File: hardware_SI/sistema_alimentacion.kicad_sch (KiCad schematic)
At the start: 29 parts

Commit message: Etq compon, C desacop, ferrita
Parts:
- added C9: 100n, symbol Device:C
- added FB1: FerriteBead, symbol Device:FerriteBead
- R10: renamed from R?; value R -> 1.5M
- R11: renamed from R?; value R -> 180k
- gave numbers to parts that had none: 27
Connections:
- net +BATT: now also C9.1
- net GND: now also J2.5 (GND), C9.2, FB1.2
- net GNDPWR: now also FB1.1; no longer J2.5 (GND)

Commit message: mod_WD, etiquetas y clocks
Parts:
- added FB?: FerriteBead, Resistor_SMD:R_0805_2012Metric_Pad1.20x1.40mm_HandSolder, symbol Device:FerriteBead
- FB1: footprint (none) -> Resistor_SMD:R_0805_2012Metric_Pad1.20x1.40mm_HandSolder
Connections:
- net GND: now also FB?.1
- net GNDPWR: now also FB?.2
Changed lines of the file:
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@@
   (junction (at 148.59 157.48) (diameter 0) (color 0 0 0 0)
+  )
+  (junction (at 113.03 185.42) (diameter 0) (color 0 0 0 0)
+  )
+  (junction (at 105.41 185.42) (diameter 0) (color 0 0 0 0)
   )
   (junction (at 137.16 167.64) (diameter 0) (color 0 0 0 0)
@@
     (stroke (width 0) (type default) (color 0 0 0 0))
   )
-  (wire (pts (xy 113.03 177.8) (xy 113.03 176.53))
+  (wire (pts (xy 113.03 185.42) (xy 113.03 176.53))
+    (stroke (width 0) (type default) (color 0 0 0 0))
+  )
+  (wire (pts (xy 113.03 189.23) (xy 113.03 185.42))
     (stroke (width 0) (type default) (color 0 0 0 0))
   )
@@
     (stroke (width 0) (type default) (color 0 0 0 0))
   )
+  (wire (pts (xy 105.41 185.42) (xy 105.41 189.23))
+    (stroke (width 0) (type default) (color 0 0 0 0))
+  )
   (wire (pts (xy 83.82 52.07) (xy 86.36 52.07))
     (stroke (width 0) (type default) (color 0 0 0 0))
@@
     (stroke (width 0) (type default) (color 0 0 0 0))
   )
-  (wire (pts (xy 105.41 176.53) (xy 105.41 177.8))
+  (wire (pts (xy 105.41 176.53) (xy 105.41 185.42))
     (stroke (width 0) (type default) (color 0 0 0 0))
   )
@@
       (effects (font (size 1.27 1.27)) (justify left bottom) hide)
     )
-    (property "Datasheet" "" (id 3) (at 86.36 49.53 0)
+    (property "Datasheet" "https://co.mouser.com/datasheet/2/609/4085fd-1268485.pdf" (id 3) (at 86.36 49.53 0)
       (effects (font (size 1.27 1.27)) (justify left bottom) hide)
     )
@@
     (pin "3")
   )
+  (symbol (lib_id "Device:FerriteBead") (at 109.22 185.42 90) (unit 1)
+    (in_bom yes) (on_board yes)
+    (property "Reference" "FB?" (id 0) (at 109.1692 177.8 90))
+    (property "Value" "FerriteBead" (id 1) (at 109.1692 180.34 90))
+    (property "Footprint" "Resistor_SMD:R_0805_2012Metric_Pad1.20x1.40mm_HandSolder" (id 2) (at 109.22 187.198 90)
+      (effects (font (size 1.27 1.27)) hide)
+    )
+    (property "Datasheet" "https://co.mouser.com/datasheet/2/396/TaiyoYuden_chipbeads01_e-1274227.pdf" (id 3) (at 109.22 185.42 0)
+      (effects (font (size 1.27 1.27)) hide)
+    )
+    (pin "1")
+    (pin "2")
+  )
   (symbol (lib_id "Device:FerriteBead") (at 62.23 135.89 90) (unit 1)
     (in_bom yes) (on_board yes)
     (property "Reference" "FB1" (id 0) (at 62.1792 128.27 90))
     (property "Value" "FerriteBead" (id 1) (at 62.1792 130.81 90))
-    (property "Footprint" "" (id 2) (at 62.23 137.668 90)
-      (effects (font (size 1.27 1.27)) hide)
-    )
-    (property "Datasheet" "~" (id 3) (at 62.23 135.89 0)
+    (property "Footprint" "Resistor_SMD:R_0805_2012Metric_Pad1.20x1.40mm_HandSolder" (id 2) (at 62.23 137.668 90)
+      (effects (font (size 1.27 1.27)) hide)
+    )
+    (property "Datasheet" "https://co.mouser.com/datasheet/2/396/TaiyoYuden_chipbeads01_e-1274227.pdf" (id 3) (at 62.23 135.89 0)
       (effects (font (size 1.27 1.27)) hide)
     )
@@
     (pin "2")
   )
-  (symbol (lib_id "power:GND") (at 105.41 177.8 0) (unit 1)
-    (in_bom yes) (on_board yes)
-    (property "Reference" "#PWR?" (id 0) (at 105.41 184.15 0)
-      (effects (font (size 1.27 1.27)) hide)
-    )
-    (property "Value" "GND" (id 1) (at 105.41 181.61 0))
-    (property "Footprint" "" (id 2) (at 105.41 177.8 0)
-      (effects (font (size 1.27 1.27)) hide)
-    )
-    (property "Datasheet" "" (id 3) (at 105.41 177.8 0)
+  (symbol (lib_id "power:GND") (at 105.41 189.23 0) (unit 1)
+    (in_bom yes) (on_board yes)
+    (property "Reference" "#PWR?" (id 0) (at 105.41 195.58 0)
+      (effects (font (size 1.27 1.27)) hide)
+    )
+    (property "Value" "GND" (id 1) (at 105.41 193.04 0))
+    (property "Footprint" "" (id 2) (at 105.41 189.23 0)
+      (effects (font (size 1.27 1.27)) hide)
+    )
+    (property "Datasheet" "" (id 3) (at 105.41 189.23 0)
       (effects (font (size 1.27 1.27)) hide)
     )
@@
     (pin "1")
   )
-  (symbol (lib_id "power:GNDPWR") (at 113.03 177.8 0) (unit 1)
-    (in_bom yes) (on_board yes)
-    (property "Reference" "#PWR?" (id 0) (at 113.03 182.88 0)
-      (effects (font (size 1.27 1.27)) hide)
-    )
-    (property "Value" "GNDPWR" (id 1) (at 113.03 181.61 0))
-    (property "Footprint" "" (id 2) (at 113.03 179.07 0)
-      (effects (font (size 1.27 1.27)) hide)
-    )
-    (property "Datasheet" "" (id 3) (at 113.03 179.07 0)
-      (effects (font (size 1.27 1.27)) hide)
-    )
+  (symbol (lib_id "power:GNDPWR") (at 113.03 189.23 0) (unit 1)
+    (in_bom yes) (on_board yes)
+    (property "Reference" "#PWR?" (id 0) (at 113.03 194.31 0)
+      (effects (font (size 1.27 1.27)) hide)
+    )
+    (property "Value" "GNDPWR" (id 1) (at 113.03 193.04 0))
+    (property "Footprint" "" (id 2) (at 113.03 190.5 0)
+      (effects (font (size 1.27 1.27)) hide)
+    )
+    (property "Datasheet" "" (id 3) (at 113.03 190.5 0)
+      (effects (font (size 1.27 1.27)) hide)
+    )

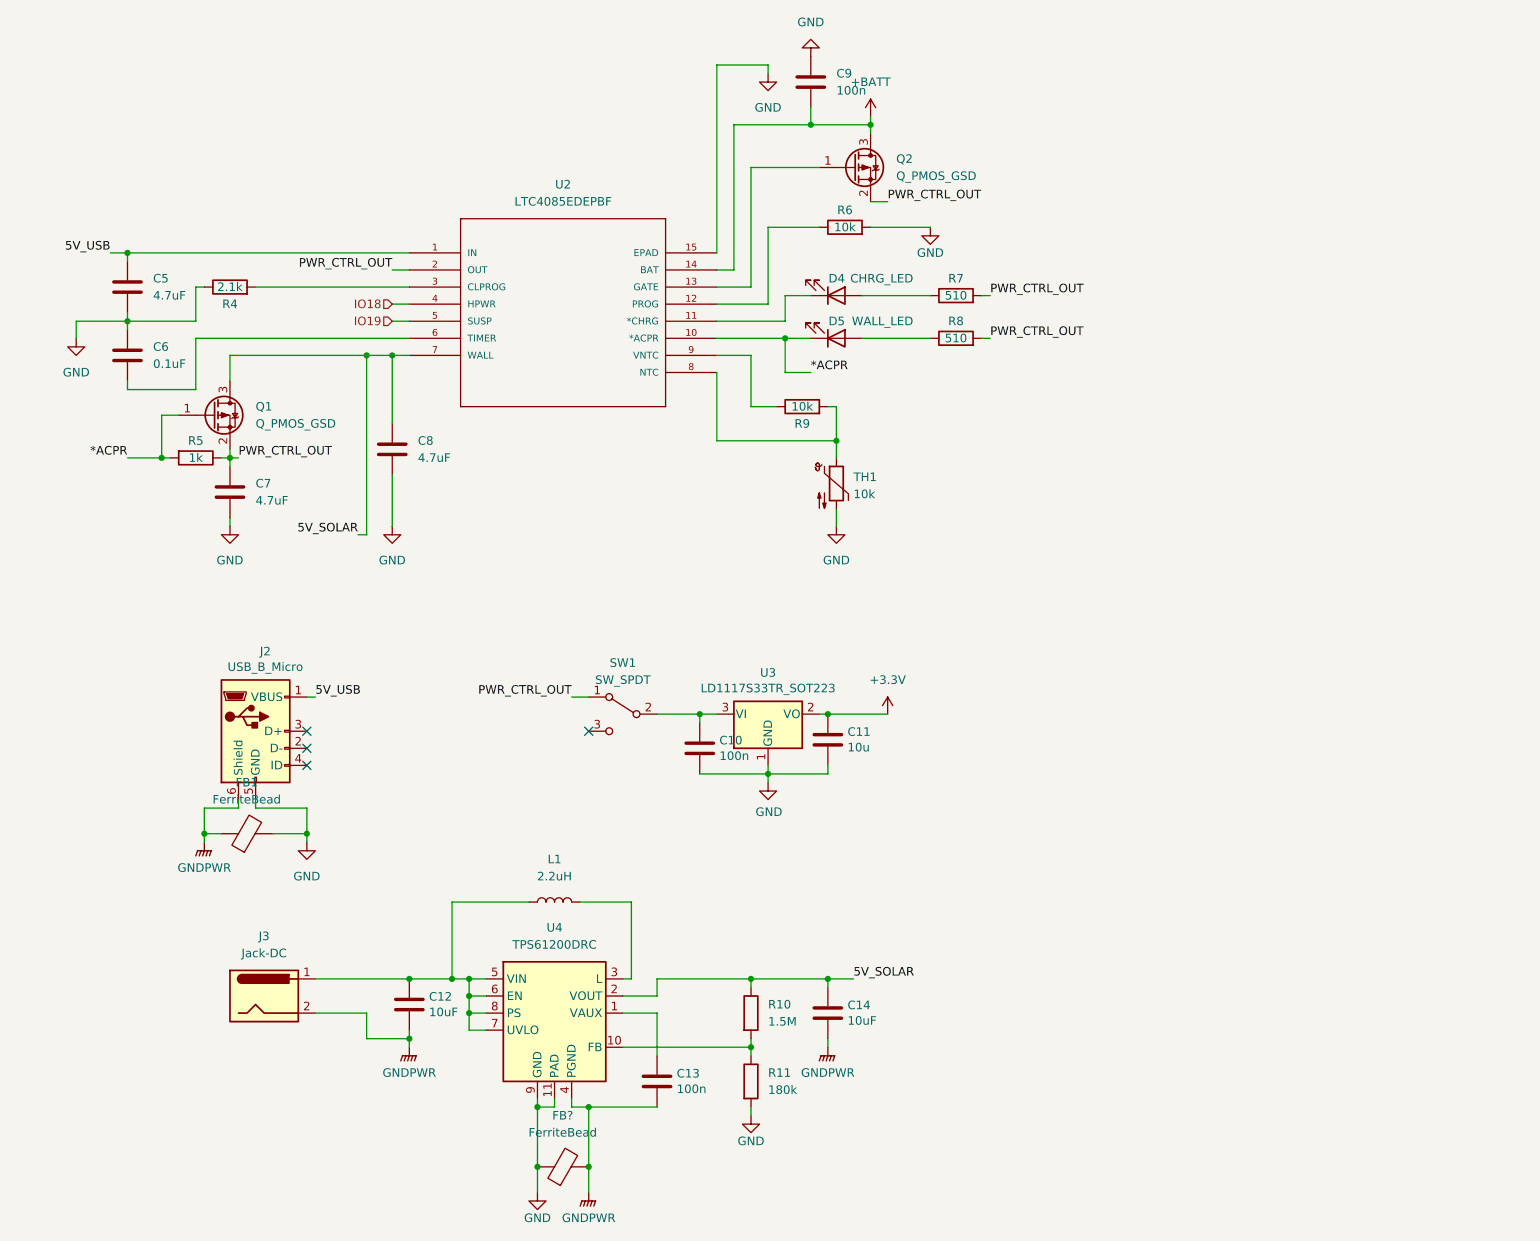
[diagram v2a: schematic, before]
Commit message: USB Serial, huellas y correcciones ERC
- Se agregaron componentes para la comunicación serial con la Omega2+.
- Se actualizaron huellas en función de la disponibilidad de los componentes.
- Se ejecutó el ERC y se solucionaron los errores mostrados.
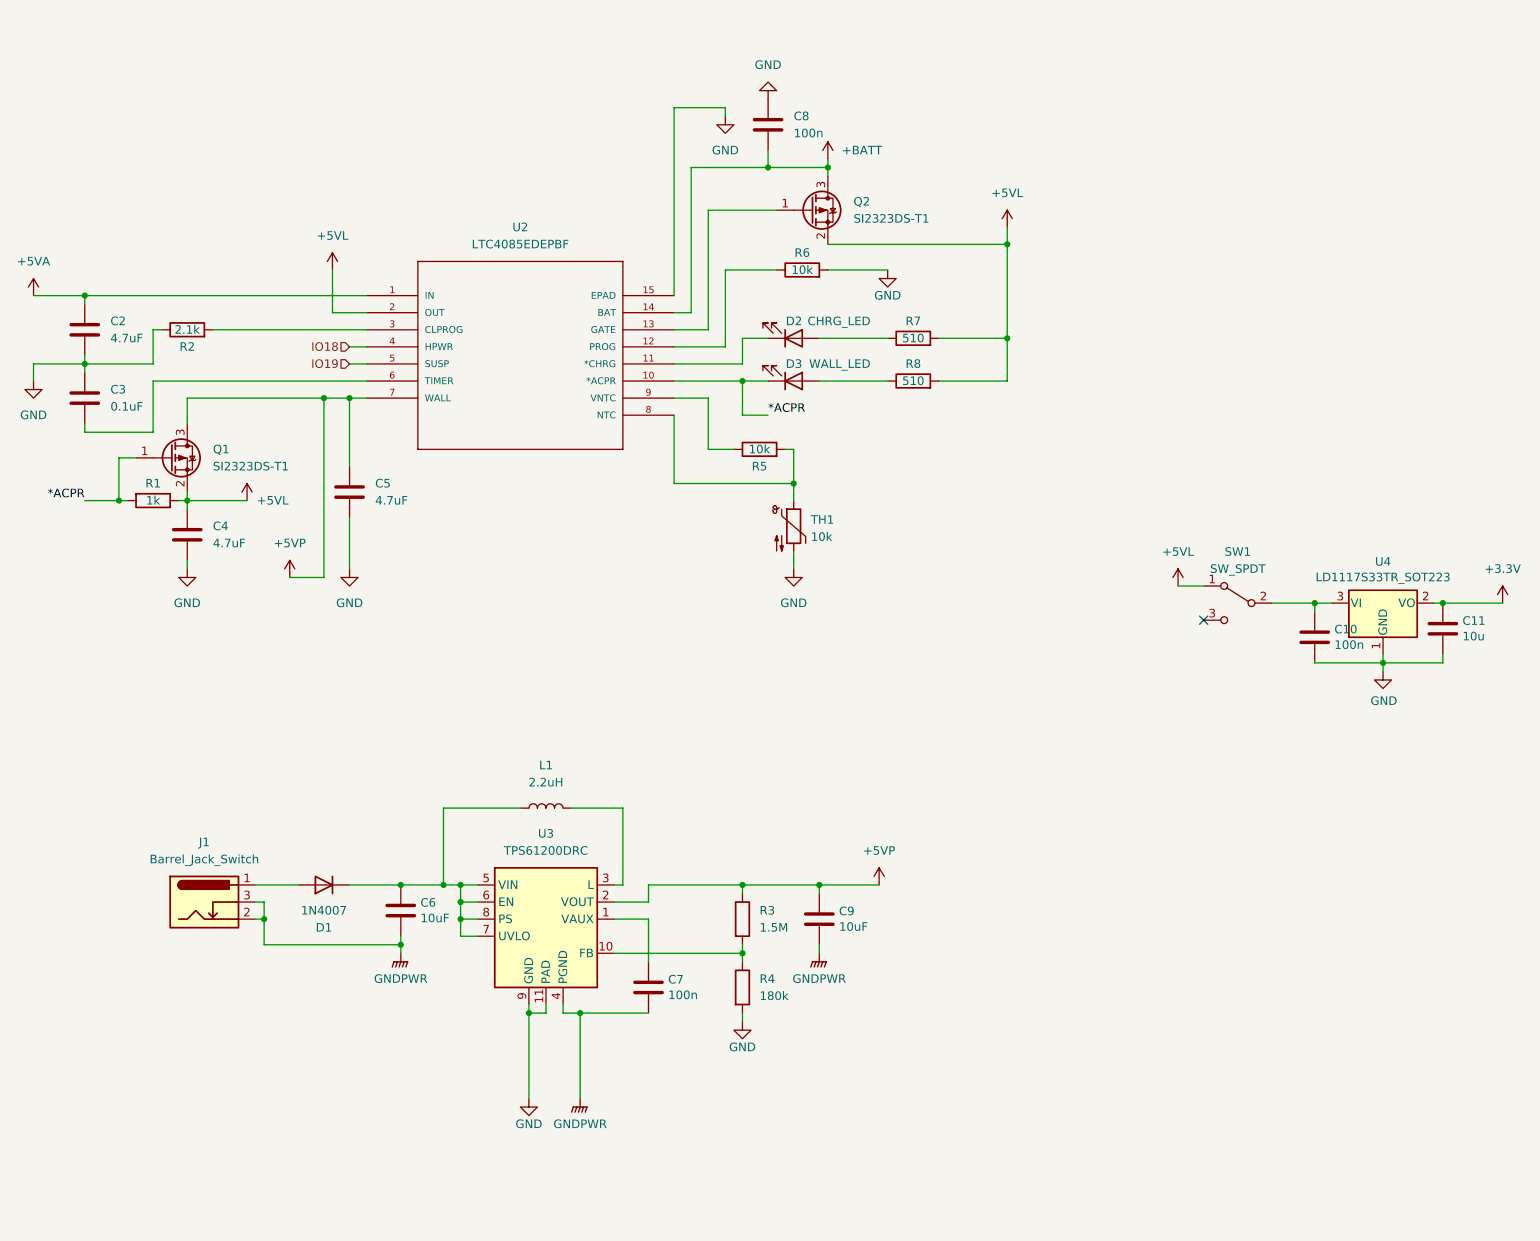
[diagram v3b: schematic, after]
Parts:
- removed FB1, FB?: FerriteBead, Resistor_SMD:R_0805_2012Metric_Pad1.20x1.40mm_HandSolder, symbol Device:FerriteBead
- removed J2: USB_B_Micro, Connector_USB:USB_Micro-B_Molex-105017-0001, symbol Connector:USB_B_Micro
- removed J3: Jack-DC, Connector_BarrelJack:BarrelJack_SwitchcraftConxall_RAPC10U_Horizontal, symbol Connector:Jack-DC
- added D1: 1N4007, Diode_SMD:D_SMA_Handsoldering, symbol Diode:1N4007
- added J1: Barrel_Jack_Switch, Connector_BarrelJack:BarrelJack_Horizontal, symbol Connector:Barrel_Jack_Switch
- Q1, Q2: value Q_PMOS_GSD -> SI2323DS-T1
- renumbered C5 to C2, C6 to C3, C7 to C4, C8 to C5, C12 to C6, C13 to C7, C9 to C8, C14 to C9, D4 to D2, D5 to D3, R5 to R1, R4 to R2, R10 to R3, R11 to R4, R9 to R5, U4 to U3, U3 to U4
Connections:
- net GNDPWR: now also J1.2, J1.3
- net at C6.1, L1.1, U3.5 (VIN)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: now also D1.1 (K)
- net 5V_SOLAR renamed +5VP
- net 5V_USB renamed +5VA
- net PWR_CTRL_OUT renamed +5VL
- new net: D1.2 (A), J1.1
- no-connect marks 4 -> 1
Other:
- moved on the sheet: C10, C11, C2, C3, C4, C5, C6, C7, C8, C9, D2, D3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

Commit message: Definiciones PCB
- Se agregan definiciones para la creación de la PCB.
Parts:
- C8: footprint (none) -> Capacitor_SMD:C_0805_2012Metric_Pad1.18x1.45mm_HandSolder
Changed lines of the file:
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@@
       (effects (font (size 1.27 1.27)) (justify right))
     )
-    (property "Footprint" "" (id 2) (at 138.7348 26.67 0)
+    (property "Footprint" "Capacitor_SMD:C_0805_2012Metric_Pad1.18x1.45mm_HandSolder" (id 2) (at 138.7348 26.67 0)
       (effects (font (size 1.27 1.27)) hide)
     )
